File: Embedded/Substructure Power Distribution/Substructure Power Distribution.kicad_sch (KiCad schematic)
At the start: 20 parts, among them J1 S JST, J2 D0 FFC, J3 D1 FFC, J4 S Pins A, J5 S Pins B, U3 SI7111EDN-T1-GE3, U4 SI7111EDN-T1-GE3

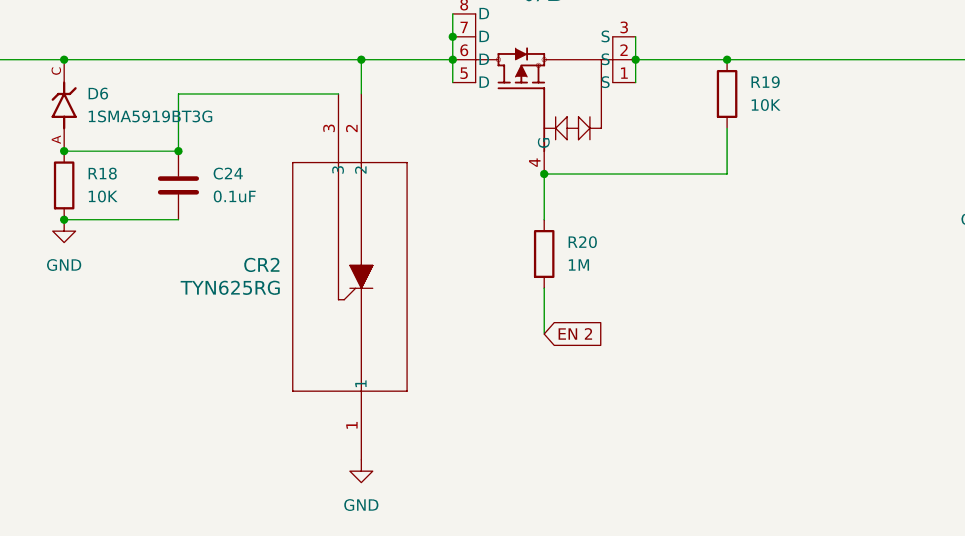
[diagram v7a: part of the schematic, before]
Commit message: Modified Thyristor (Replaced component)
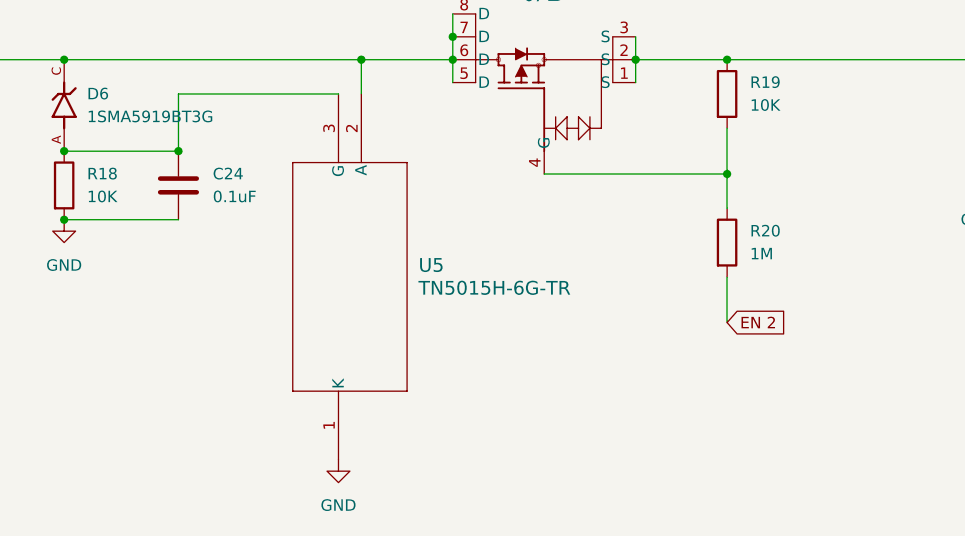
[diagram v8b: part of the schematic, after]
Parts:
- removed CR2: TYN625RG, Thyristor TYN:TO-220AB_STM, symbol Thyristor TYN:TYN625RG
- added U5: TN5015H-6G-TR, Thyristor TN5:D2PAK_T2550_STM-M, symbol Thyristor TN5:TN5015H-6G-TR
- C24: footprint Capacitor_SMD:C_0402_1005Metric_Pad0.74x0.62mm_HandSolder -> Capacitor_SMD:C_0603_1608Metric_Pad1.08x0.95mm_HandSolder
- R17, R18, R19, R20, R21: footprint Resistor_SMD:R_0402_1005Metric_Pad0.72x0.64mm_HandSolder -> Resistor_SMD:R_0603_1608Metric_Pad0.98x0.95mm_HandSolder
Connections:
- net GND: now also U5.1 (K)
- net at D6.C, F2.2, U4.5 (D)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: now also U5.2 (A)
- net at C24.1, D6.A, R18.1: now also U5.3 (G)
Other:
- moved on the sheet: R20
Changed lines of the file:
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@@
 	)
 	(junction
-		(at 218.44 127)
-		(diameter 0)
-		(color 0 0 0 0)
-	)
-	(junction
 		(at 41.91 127)
 		(diameter 0)
@@
 	)
 	(junction
+		(at 238.76 127)
+		(diameter 0)
+		(color 0 0 0 0)
+	)
+	(junction
 		(at 228.6 114.3)
 		(diameter 0)
@@
 	(wire
 		(pts
+			(xy 238.76 127) (xy 218.44 127)
+		)
+		(stroke
+			(width 0)
+			(type default)
+		)
+	)
+	(wire
+		(pts
 			(xy 177.8 118.11) (xy 177.8 124.46)
 		)
@@
 	(wire
 		(pts
-			(xy 91.44 127) (xy 91.44 124.46)
+			(xy 238.76 127) (xy 238.76 130.81)
 		)
 		(stroke
@@
 	(wire
 		(pts
-			(xy 218.44 144.78) (xy 218.44 139.7)
+			(xy 91.44 127) (xy 91.44 124.46)
 		)
 		(stroke
@@
 	(wire
 		(pts
-			(xy 71.12 129.54) (xy 71.12 127)
+			(xy 238.76 143.51) (xy 238.76 138.43)
 		)
 		(stroke
@@
 	(wire
 		(pts
-			(xy 218.44 132.08) (xy 218.44 127)
+			(xy 71.12 129.54) (xy 71.12 127)
 		)
 		(stroke
@@
 	(wire
 		(pts
-			(xy 238.76 127) (xy 218.44 127)
-		)
-		(stroke
-			(width 0)
-			(type default)
-		)
-	)
-	(wire
-		(pts
 			(xy 228.6 114.3) (xy 238.76 114.3)
 		)
@@
 	(global_label "EN 2"
 		(shape input)
-		(at 218.44 144.78 0)
+		(at 238.76 143.51 0)
 		(fields_autoplaced yes)
 		(effects
@@
 		)
 		(property "Intersheetrefs" "${INTERSHEET_REFS}"
-			(at 226.0818 144.78 0)
+			(at 246.4018 143.51 0)
 			(effects
 				(font
@@
 			)
 		)
-		(property "Footprint" "Resistor_SMD:R_0402_1005Metric_Pad0.72x0.64mm_HandSolder"
+		(property "Footprint" "Resistor_SMD:R_0603_1608Metric_Pad0.98x0.95mm_HandSolder"
 			(at 79.502 147.32 90)
 			(effects
@@
 			)
 		)
-		(property "Footprint" "Resistor_SMD:R_0402_1005Metric_Pad0.72x0.64mm_HandSolder"
+		(property "Footprint" "Resistor_SMD:R_0603_1608Metric_Pad0.98x0.95mm_HandSolder"
 			(at 236.982 118.11 90)
 			(effects
@@
 	(symbol
 		(lib_id "Device:R")
-		(at 218.44 135.89 0)
+		(at 238.76 134.62 0)
 		(unit 1)
 		(exclude_from_sim no)
@@
 		(fields_autoplaced yes)
 		(property "Reference" "R20"
-			(at 220.98 134.6199 0)
+			(at 241.3 133.3499 0)
 			(effects
 				(font
@@
 		)
 		(property "Value" "1M"
-			(at 220.98 137.1599 0)
+			(at 241.3 135.8899 0)
 			(effects
 				(font
@@
 			)
 		)
-		(property "Footprint" "Resistor_SMD:R_0402_1005Metric_Pad0.72x0.64mm_HandSolder"
-			(at 216.662 135.89 90)
+		(property "Footprint" "Resistor_SMD:R_0603_1608Metric_Pad0.98x0.95mm_HandSolder"
+			(at 236.982 134.62 90)
 			(effects
 				(font
@@
 		)
 		(property "Datasheet" "~"
-			(at 218.44 135.89 0)
+			(at 238.76 134.62 0)
 			(effects
 				(font
@@
 		)
 		(property "Description" "Resistor"
-			(at 218.44 135.89 0)
+			(at 238.76 134.62 0)
 			(effects
 				(font
@@
 	)
 	(symbol
-		(lib_id "Thyristor TYN:TYN625RG")
-		(at 198.12 158.75 270)
-		(mirror x)
-		(unit 1)
-		(exclude_from_sim no)
-		(in_bom yes)
-		(on_board yes)
-		(dnp no)
-		(property "Reference" "CR2"
-			(at 189.23 137.1599 90)
-			(effects
-				(font
-					(size 1.524 1.524)
-				)
-				(justify right)
-			)
-		)
-		(property "Value" "TYN625RG"
-			(at 189.23 139.6999 90)
-			(effects
-				(font
-					(size 1.524 1.524)
-				)
-				(justify right)
-			)
-		)
-		(property "Footprint" "Thyristor TYN:TO-220AB_STM"
-			(at 198.12 158.75 0)
-			(effects
-				(font
-					(size 1.27 1.27)
-					(italic yes)
-				)
-				(hide yes)
-			)
-		)
-		(property "Datasheet" "https://www.st.com/resource/en/datasheet/tn2540.pdf"
-			(at 198.12 158.75 0)
-			(effects
-				(font
-					(size 1.27 1.27)
-					(italic yes)
-				)
-				(hide yes)
-			)
-		)
-		(property "Description" ""
-			(at 198.12 158.75 0)
-			(effects
-				(font
-					(size 1.27 1.27)
-				)
-				(hide yes)
-			)
-		)
-		(pin "3"
-		)
-		(pin "1"
-		)
-		(pin "2"
-		)
-		(instances
-			(project ""
-				(path "/6e7c3700-4b7d-4b10-b755-ccb609125a98"
-					(reference "CR2")
-					(unit 1)
-				)
-			)
-		)
-	)
-	(symbol
 		(lib_id "power:GND")
 		(at 132.08 63.5 90)
@@
 			)
 		)
-		(property "Footprint" "Resistor_SMD:R_0402_1005Metric_Pad0.72x0.64mm_HandSolder"
+		(property "Footprint" "Resistor_SMD:R_0603_1608Metric_Pad0.98x0.95mm_HandSolder"
 			(at 163.322 128.27 90)
 			(effects
@@
 			)
 		)
-		(property "Footprint" "Resistor_SMD:R_0402_1005Metric_Pad0.72x0.64mm_HandSolder"
+		(property "Footprint" "Resistor_SMD:R_0603_1608Metric_Pad0.98x0.95mm_HandSolder"
 			(at 73.66 141.478 90)
 			(effects
@@
 	(symbol
 		(lib_id "power:GND")
-		(at 198.12 158.75 0)
+		(at 195.58 158.75 0)
 		(unit 1)
 		(exclude_from_sim no)
@@
 		(fields_autoplaced yes)
 		(property "Reference" "#PWR042"
-			(at 198.12 165.1 0)
+			(at 195.58 165.1 0)
 			(effects
 				(font
@@
 		)
 		(property "Value" "GND"
-			(at 198.12 163.83 0)
+			(at 195.58 163.83 0)
 			(effects
 				(font
@@
 		)
 		(property "Footprint" ""
-			(at 198.12 158.75 0)
+			(at 195.58 158.75 0)
 			(effects
 				(font
@@
 		)
 		(property "Datasheet" ""
-			(at 198.12 158.75 0)
+			(at 195.58 158.75 0)
 			(effects
 				(font
@@
 		)
 		(property "Description" "Power symbol creates a global label with name \"GND\" , ground"
-			(at 198.12 158.75 0)
+			(at 195.58 158.75 0)
 			(effects
 				(font
@@
 			)
 		)
-		(property "Footprint" "Capacitor_SMD:C_0402_1005Metric_Pad0.74x0.62mm_HandSolder"
+		(property "Footprint" "Capacitor_SMD:C_0603_1608Metric_Pad1.08x0.95mm_HandSolder"
 			(at 178.7652 132.08 0)
 			(effects
@@
 					(unit 1)
 				)
+			)
+		)
+	)
+	(symbol
+		(lib_id "Thyristor TN5:TN5015H-6G-TR")
+		(at 195.58 158.75 90)
+		(unit 1)
+		(exclude_from_sim no)
+		(in_bom yes)
+		(on_board yes)
+		(dnp no)
+		(fields_autoplaced yes)
+		(property "Reference" "U5"
+			(at 204.47 137.1599 90)
+			(effects
+				(font
+					(size 1.524 1.524)
+				)
+				(justify right)
+			)
+		)
+		(property "Value" "TN5015H-6G-TR"
+			(at 204.47 139.6999 90)
+			(effects
+				(font
+					(size 1.524 1.524)
+				)
+				(justify right)
+			)
+		)
+		(property "Footprint" "Thyristor TN5:D2PAK_T2550_STM-M"
+			(at 195.58 158.75 0)
+			(effects
+				(font
+					(size 1.27 1.27)
+					(italic yes)
+				)
+				(hide yes)
+			)
+		)
+		(property "Datasheet" "https://www.st.com/resource/en/datasheet/tn5015h-6g.pdf"
+			(at 195.58 158.75 0)
+			(effects
+				(font
+					(size 1.27 1.27)
+					(italic yes)
+				)
+				(hide yes)
+			)
+		)
+		(property "Description" ""
+			(at 195.58 158.75 0)
+			(effects
+				(font
+					(size 1.27 1.27)
+				)
+				(hide yes)
+			)
+		)
+		(pin "1"
+		)
+		(pin "2"
+		)
+		(pin "3"
+		)
+		(instances
+			(project ""
+				(path "/6e7c3700-4b7d-4b10-b755-ccb609125a98"
+					(reference "U5")
+					(unit 1)
+				)
